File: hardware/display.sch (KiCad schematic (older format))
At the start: 16 parts

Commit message: hardware development
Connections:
- net S1_A: now also U?.7 (A)
- net S1_B: now also U?.6 (B)
- net S1_C: now also U?.4 (C)
- net S1_D: now also U?.2 (D)
- net S1_DP: now also U?.5 (DP)
- net S1_E: now also U?.1 (E)
- net S1_F: now also U?.9 (F)
- net S1_G: now also U?.10 (G)
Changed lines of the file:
@@
 $Descr A4 11693 8268
 encoding utf-8
-Sheet 3 3
+Sheet 2 4
 Title ""
 Date ""
@@
 Wire Wire Line
 	7400 5250 7700 5250
+Wire Wire Line
+	2100 2850 2350 2850
+Wire Wire Line
+	2350 2950 2100 2950
+Wire Wire Line
+	2100 3050 2350 3050
+Wire Wire Line
+	2350 3150 2100 3150
+Wire Wire Line
+	2350 3250 2100 3250
+Wire Wire Line
+	2100 3350 2350 3350
+Wire Wire Line
+	2350 3450 2100 3450
+Wire Wire Line
+	2100 3550 2350 3550
 $EndSCHEMATC

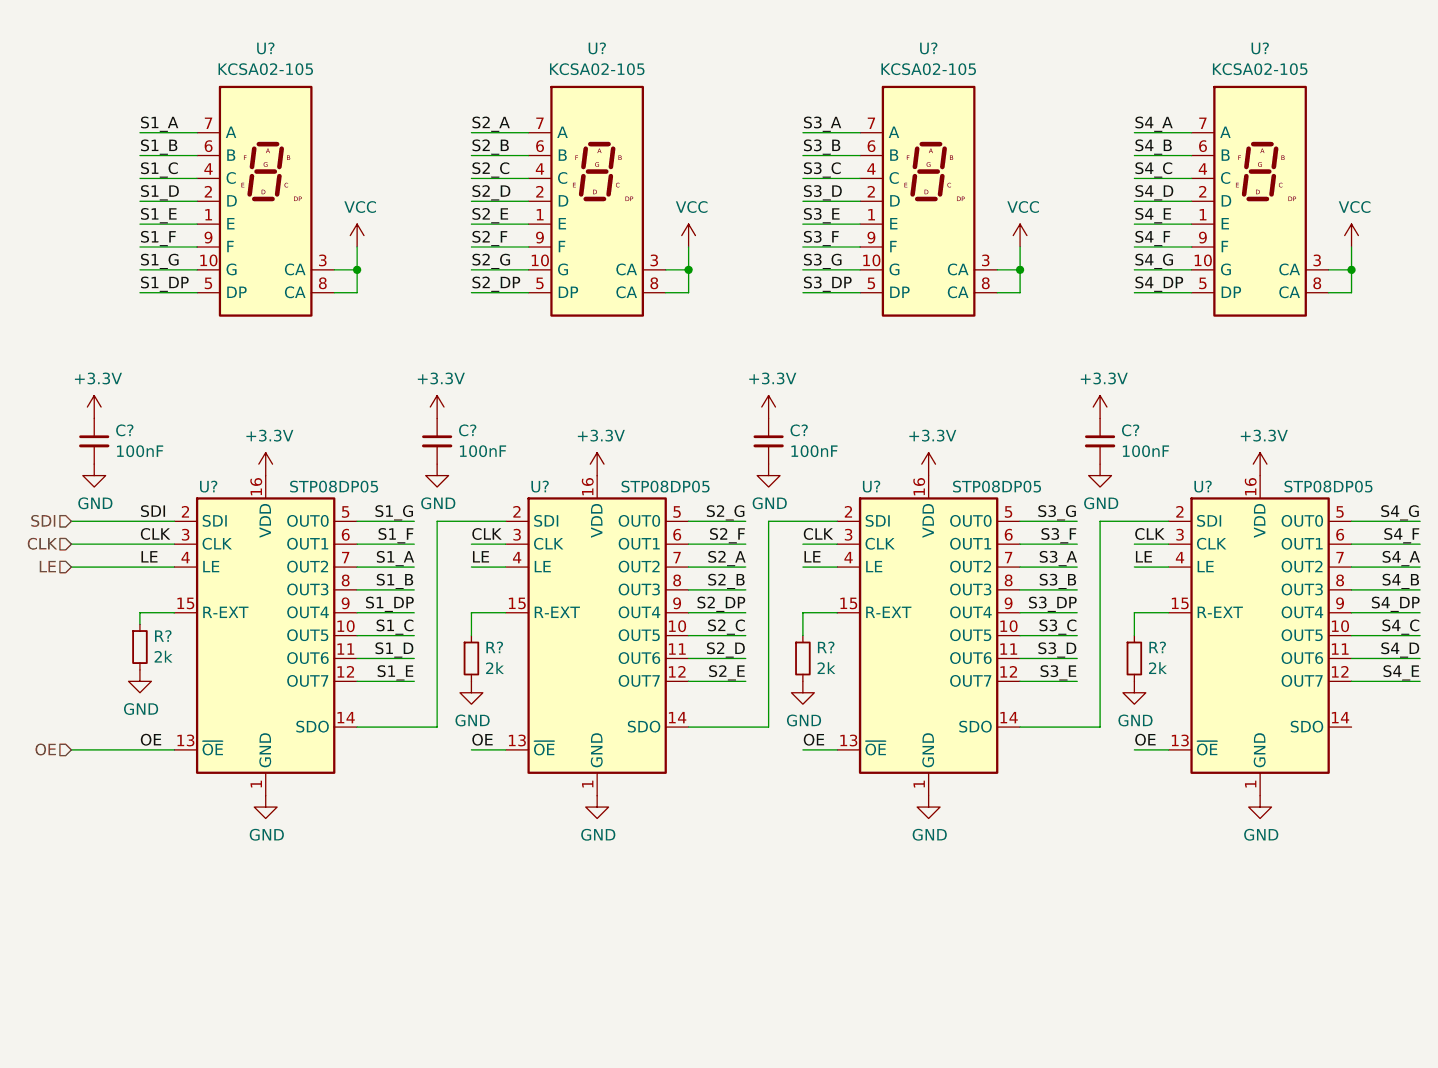
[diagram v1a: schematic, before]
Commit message: schematic should be done, pcb is next
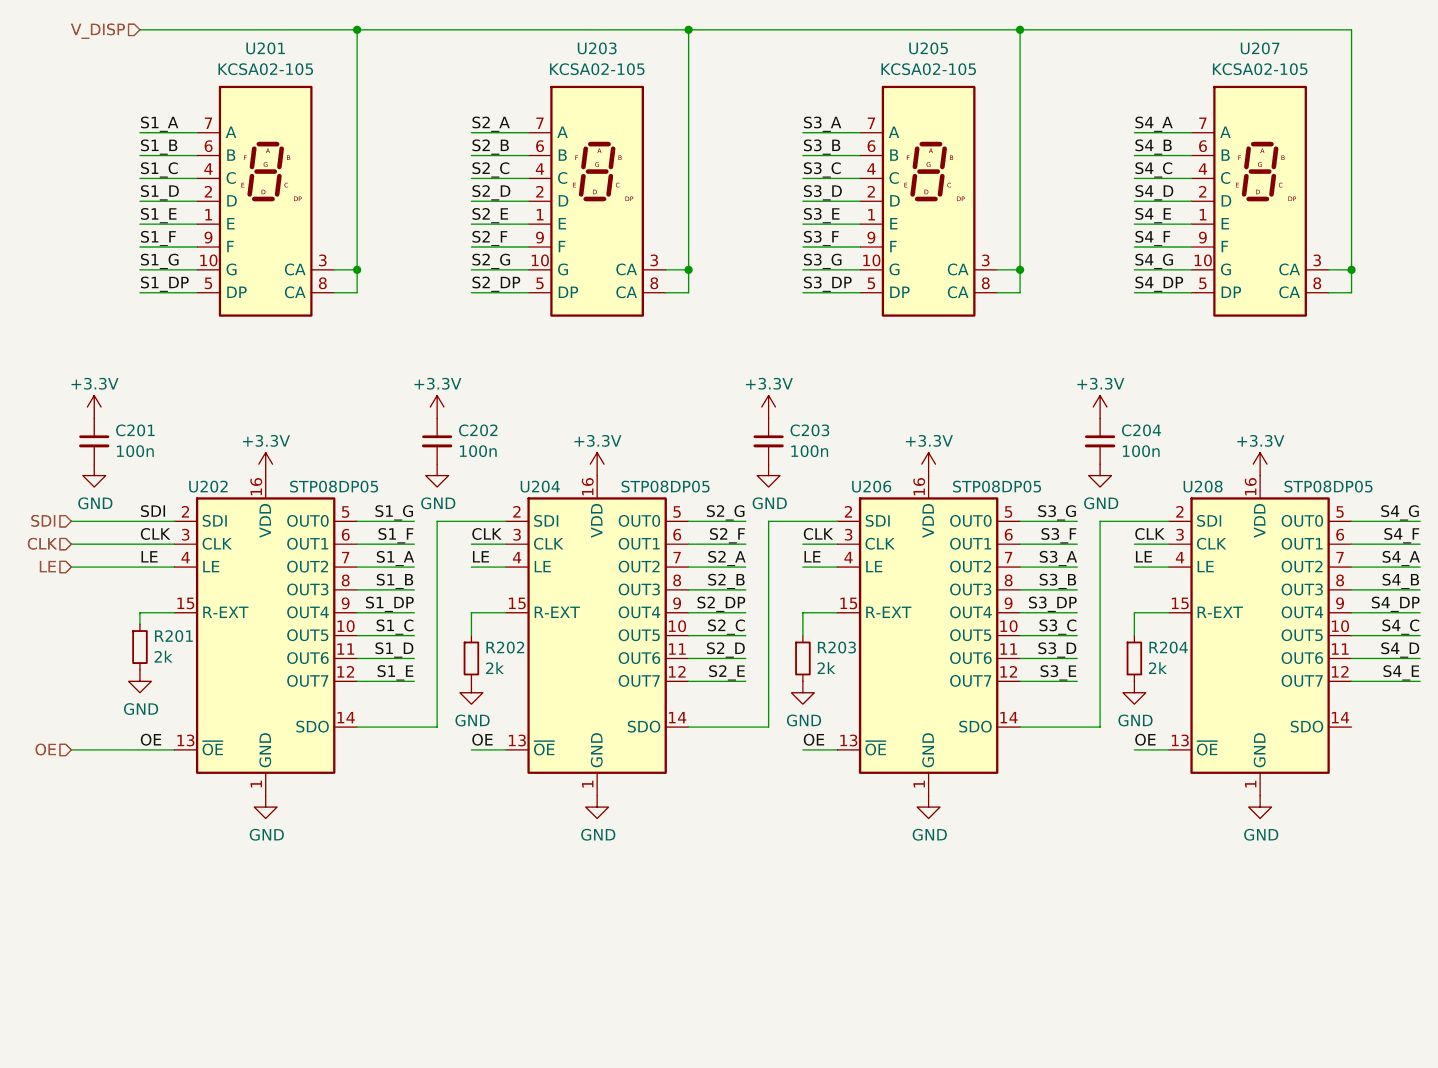
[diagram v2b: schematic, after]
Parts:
- C201, C202, C203, C204: renamed from C?; value 100nF -> 100n; Manufacturer (none) -> KEMET; Order https://www.digikey.at/product-detail/de/kemet/C0603C104M4R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 -> https://www.mouser.at/ProductDetail/80-C0603C104M4R
- R201, R202, R203, R204: renamed from R?; Manufacturer (none) -> Panasonic; Order https://www.digikey.at/product-detail/de/panasonic-electron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 -> https://www.mouser.at/ProductDetail/667-ERJ-PA3F2001V
- U201, U203, U205, U207: renamed from U?; Manufacturer (none) -> Kingbright; Order https://www.digikey.at/product-detail/de/XZFMDK05A/1497-109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 -> https://www.mouser.at/ProductDetail/604-ACSA02-41SURKWA
- U202, U204, U206, U208: renamed from U?; Manufacturer (none) -> STMicroelectornics; Order https://www.digikey.at/product-detail/de/STP08DP05TTR/497-6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 -> https://www.mouser.at/ProductDetail/511-STP08DP05TTR; Part Number (none) -> STP08DP05TTR
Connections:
- net VCC renamed V_DISP

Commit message: wip hw
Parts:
- C201, C202, C203, C204: footprint Capacitor_SMD:C_0603_1608Metric_Pad1.05x0.95mm_HandSolder -> Capacitor_SMD:C_0603_1608Metric
- R201, R202, R203, R204: footprint Resistor_SMD:R_0603_1608Metric_Pad1.05x0.95mm_HandSolder -> Resistor_SMD:R_0603_1608Metric
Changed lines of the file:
@@
 F 0 "R201" H 2159 5146 50  0000 L CNN
 F 1 "2k" H 2159 5055 50  0000 L CNN
-F 2 "Resistor_SMD:R_0603_1608Metric_Pad1.05x0.95mm_HandSolder" H 2100 5100 50  0001 C CNN
+F 2 "Resistor_SMD:R_0603_1608Metric" H 2100 5100 50  0001 C CNN
 F 3 "https://www.mouser.at/datasheet/2/315/AOA0000C331-1141874.pdf" H 2100 5100 50  0001 C CNN
 F 4 "https://www.mouser.at/ProductDetail/667-ERJ-PA3F2001V" H 2100 5100 50  0001 C CNN "Order"
@@
 F 0 "C201" H 1992 4246 50  0000 L CNN
 F 1 "100n" H 1992 4155 50  0000 L CNN
-F 2 "Capacitor_SMD:C_0603_1608Metric_Pad1.05x0.95mm_HandSolder" H 1900 4200 50  0001 C CNN
+F 2 "Capacitor_SMD:C_0603_1608Metric" H 1900 4200 50  0001 C CNN
 F 3 "https://www.mouser.at/datasheet/2/212/KEM_C1002_X7R_SMD-1102033.pdf" H 1900 4200 50  0001 C CNN
 F 4 "https://www.mouser.at/ProductDetail/80-C0603C104M4R" H 1900 4200 50  0001 C CNN "Order"
@@
 F 0 "R202" H 3609 5196 50  0000 L CNN
 F 1 "2k" H 3609 5105 50  0000 L CNN
-F 2 "Resistor_SMD:R_0603_1608Metric_Pad1.05x0.95mm_HandSolder" H 3550 5150 50  0001 C CNN
+F 2 "Resistor_SMD:R_0603_1608Metric" H 3550 5150 50  0001 C CNN
 F 3 "https://www.mouser.at/datasheet/2/315/AOA0000C331-1141874.pdf" H 3550 5150 50  0001 C CNN
 F 4 "https://www.mouser.at/ProductDetail/667-ERJ-PA3F2001V" H 3550 5150 50  0001 C CNN "Order"
@@
 F 0 "R203" H 5059 5196 50  0000 L CNN
 F 1 "2k" H 5059 5105 50  0000 L CNN
-F 2 "Resistor_SMD:R_0603_1608Metric_Pad1.05x0.95mm_HandSolder" H 5000 5150 50  0001 C CNN
+F 2 "Resistor_SMD:R_0603_1608Metric" H 5000 5150 50  0001 C CNN
 F 3 "https://www.mouser.at/datasheet/2/315/AOA0000C331-1141874.pdf" H 5000 5150 50  0001 C CNN
 F 4 "https://www.mouser.at/ProductDetail/667-ERJ-PA3F2001V" H 5000 5150 50  0001 C CNN "Order"
@@
 F 0 "R204" H 6509 5196 50  0000 L CNN
 F 1 "2k" H 6509 5105 50  0000 L CNN
-F 2 "Resistor_SMD:R_0603_1608Metric_Pad1.05x0.95mm_HandSolder" H 6450 5150 50  0001 C CNN
+F 2 "Resistor_SMD:R_0603_1608Metric" H 6450 5150 50  0001 C CNN
 F 3 "https://www.mouser.at/datasheet/2/315/AOA0000C331-1141874.pdf" H 6450 5150 50  0001 C CNN
 F 4 "https://www.mouser.at/ProductDetail/667-ERJ-PA3F2001V" H 6450 5150 50  0001 C CNN "Order"
@@
 F 0 "C202" H 3492 4246 50  0000 L CNN
 F 1 "100n" H 3492 4155 50  0000 L CNN
-F 2 "Capacitor_SMD:C_0603_1608Metric_Pad1.05x0.95mm_HandSolder" H 3400 4200 50  0001 C CNN
+F 2 "Capacitor_SMD:C_0603_1608Metric" H 3400 4200 50  0001 C CNN
 F 3 "https://www.mouser.at/datasheet/2/212/KEM_C1002_X7R_SMD-1102033.pdf" H 3400 4200 50  0001 C CNN
 F 4 "https://www.mouser.at/ProductDetail/80-C0603C104M4R" H 3400 4200 50  0001 C CNN "Order"
@@
 F 0 "C203" H 4942 4246 50  0000 L CNN
 F 1 "100n" H 4942 4155 50  0000 L CNN
-F 2 "Capacitor_SMD:C_0603_1608Metric_Pad1.05x0.95mm_HandSolder" H 4850 4200 50  0001 C CNN
+F 2 "Capacitor_SMD:C_0603_1608Metric" H 4850 4200 50  0001 C CNN
 F 3 "https://www.mouser.at/datasheet/2/212/KEM_C1002_X7R_SMD-1102033.pdf" H 4850 4200 50  0001 C CNN
 F 4 "https://www.mouser.at/ProductDetail/80-C0603C104M4R" H 4850 4200 50  0001 C CNN "Order"
@@
 F 0 "C204" H 6392 4246 50  0000 L CNN
 F 1 "100n" H 6392 4155 50  0000 L CNN
-F 2 "Capacitor_SMD:C_0603_1608Metric_Pad1.05x0.95mm_HandSolder" H 6300 4200 50  0001 C CNN
+F 2 "Capacitor_SMD:C_0603_1608Metric" H 6300 4200 50  0001 C CNN
 F 3 "https://www.mouser.at/datasheet/2/212/KEM_C1002_X7R_SMD-1102033.pdf" H 6300 4200 50  0001 C CNN
 F 4 "https://www.mouser.at/ProductDetail/80-C0603C104M4R" H 6300 4200 50  0001 C CNN "Order"

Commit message: finished routing
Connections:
- no-connect marks 0 -> 1
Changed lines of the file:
@@
 Wire Wire Line
 	5950 2400 7400 2400
+NoConn ~ 7400 5450
 $EndSCHEMATC

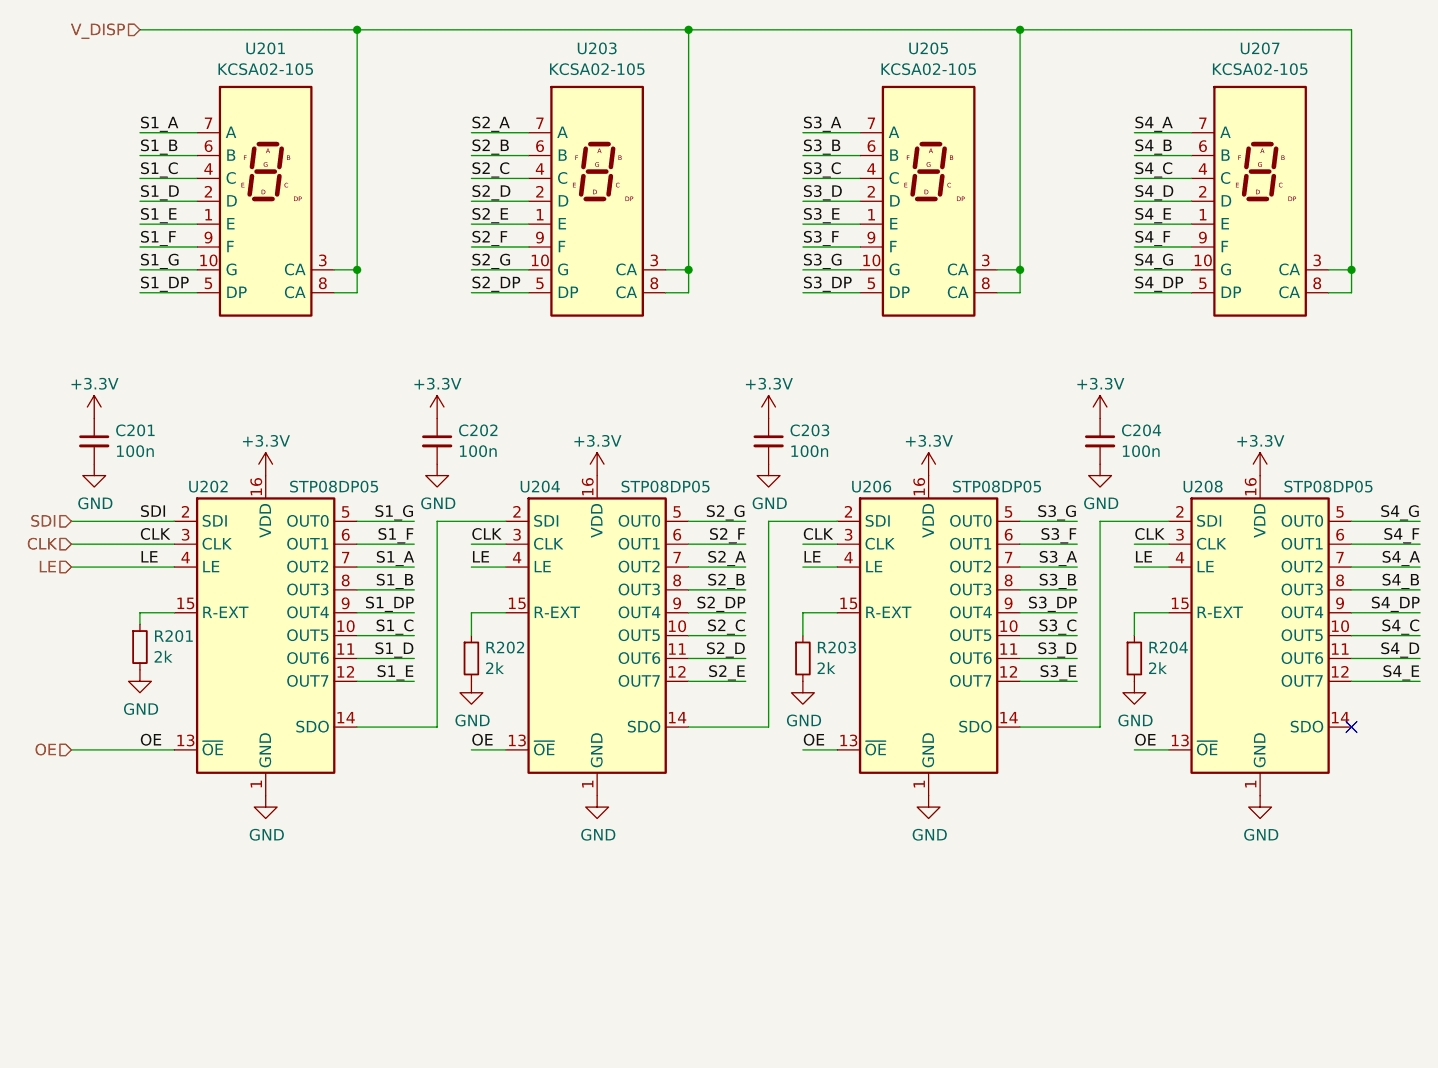
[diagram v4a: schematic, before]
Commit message: calc current consumption
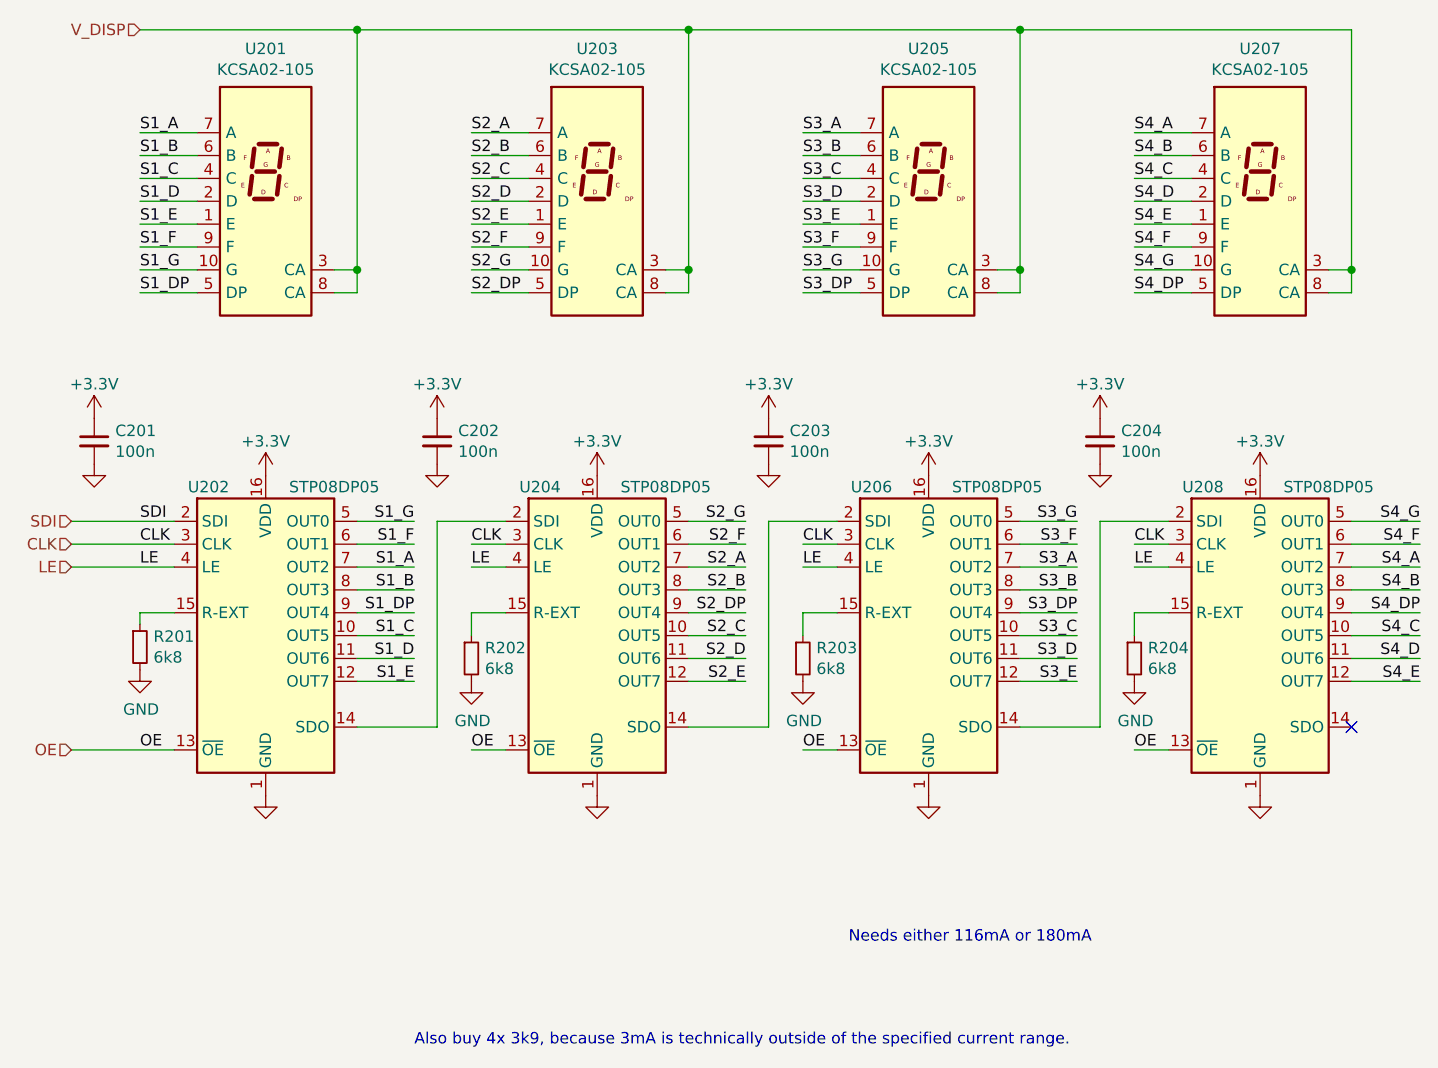
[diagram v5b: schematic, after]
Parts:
- R201, R202, R203, R204: value 2k -> 6k8
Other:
- note added: "Also buy 4x 3k9, because 3mA is technically outside of the specified current range."
- note added: "Needs either 116mA or 180mA"
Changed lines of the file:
@@
 AR Path="/60633D5C/60642EB2" Ref="R201"  Part="1"
 F 0 "R201" H 2159 5146 50  0000 L CNN
-F 1 "2k" H 2159 5055 50  0000 L CNN
+F 1 "6k8" H 2159 5055 50  0000 L CNN
 F 2 "Resistor_SMD:R_0603_1608Metric" H 2100 5100 50  0001 C CNN
 F 3 "https://www.mouser.at/datasheet/2/315/AOA0000C331-1141874.pdf" H 2100 5100 50  0001 C CNN
@@
 AR Path="/60633D5C/60642EC3" Ref="#PWR0102"  Part="1"
 F 0 "#PWR0102" H 1900 4050 50  0001 C CNN
-F 1 "GND" H 1905 4127 50  0000 C CNN
+F 1 "GND" H 1905 4127 50  0001 C CNN
 F 2 "" H 1900 4300 50  0001 C CNN
 F 3 "" H 1900 4300 50  0001 C CNN
@@
 AR Path="/60633D5C/60642EC9" Ref="#PWR0103"  Part="1"
 F 0 "#PWR0103" H 2650 5500 50  0001 C CNN
-F 1 "GND" H 2655 5577 50  0000 C CNN
+F 1 "GND" H 2655 5577 50  0001 C CNN
 F 2 "" H 2650 5750 50  0001 C CNN
 F 3 "" H 2650 5750 50  0001 C CNN
@@
 AR Path="/60633D5C/60642EFF" Ref="#PWR0108"  Part="1"
 F 0 "#PWR0108" H 4100 5500 50  0001 C CNN
-F 1 "GND" H 4105 5577 50  0000 C CNN
+F 1 "GND" H 4105 5577 50  0001 C CNN
 F 2 "" H 4100 5750 50  0001 C CNN
 F 3 "" H 4100 5750 50  0001 C CNN
@@
 AR Path="/60633D5C/60642F0C" Ref="R202"  Part="1"
 F 0 "R202" H 3609 5196 50  0000 L CNN
-F 1 "2k" H 3609 5105 50  0000 L CNN
+F 1 "6k8" H 3609 5105 50  0000 L CNN
 F 2 "Resistor_SMD:R_0603_1608Metric" H 3550 5150 50  0001 C CNN
 F 3 "https://www.mouser.at/datasheet/2/315/AOA0000C331-1141874.pdf" H 3550 5150 50  0001 C CNN
@@
 AR Path="/60633D5C/60642F27" Ref="#PWR0111"  Part="1"
 F 0 "#PWR0111" H 5550 5500 50  0001 C CNN
-F 1 "GND" H 5555 5577 50  0000 C CNN
+F 1 "GND" H 5555 5577 50  0001 C CNN
 F 2 "" H 5550 5750 50  0001 C CNN
 F 3 "" H 5550 5750 50  0001 C CNN
@@
 AR Path="/60633D5C/60642F34" Ref="R203"  Part="1"
 F 0 "R203" H 5059 5196 50  0000 L CNN
-F 1 "2k" H 5059 5105 50  0000 L CNN
+F 1 "6k8" H 5059 5105 50  0000 L CNN
 F 2 "Resistor_SMD:R_0603_1608Metric" H 5000 5150 50  0001 C CNN
 F 3 "https://www.mouser.at/datasheet/2/315/AOA0000C331-1141874.pdf" H 5000 5150 50  0001 C CNN
@@
 AR Path="/60633D5C/60642F4F" Ref="#PWR0114"  Part="1"
 F 0 "#PWR0114" H 7000 5500 50  0001 C CNN
-F 1 "GND" H 7005 5577 50  0000 C CNN
+F 1 "GND" H 7005 5577 50  0001 C CNN
 F 2 "" H 7000 5750 50  0001 C CNN
 F 3 "" H 7000 5750 50  0001 C CNN
@@
 AR Path="/60633D5C/60642F5C" Ref="R204"  Part="1"
 F 0 "R204" H 6509 5196 50  0000 L CNN
-F 1 "2k" H 6509 5105 50  0000 L CNN
+F 1 "6k8" H 6509 5105 50  0000 L CNN
 F 2 "Resistor_SMD:R_0603_1608Metric" H 6450 5150 50  0001 C CNN
 F 3 "https://www.mouser.at/datasheet/2/315/AOA0000C331-1141874.pdf" H 6450 5150 50  0001 C CNN
@@
 AR Path="/60633D5C/606457A9" Ref="#PWR0116"  Part="1"
 F 0 "#PWR0116" H 3400 4050 50  0001 C CNN
-F 1 "GND" H 3405 4127 50  0000 C CNN
+F 1 "GND" H 3405 4127 50  0001 C CNN
 F 2 "" H 3400 4300 50  0001 C CNN
 F 3 "" H 3400 4300 50  0001 C CNN
@@
 AR Path="/60633D5C/60646EB7" Ref="#PWR0118"  Part="1"
 F 0 "#PWR0118" H 4850 4050 50  0001 C CNN
-F 1 "GND" H 4855 4127 50  0000 C CNN
+F 1 "GND" H 4855 4127 50  0001 C CNN
 F 2 "" H 4850 4300 50  0001 C CNN
 F 3 "" H 4850 4300 50  0001 C CNN
@@
 AR Path="/60633D5C/60647DB5" Ref="#PWR0120"  Part="1"
 F 0 "#PWR0120" H 6300 4050 50  0001 C CNN
-F 1 "GND" H 6305 4127 50  0000 C CNN
+F 1 "GND" H 6305 4127 50  0001 C CNN
 F 2 "" H 6300 4300 50  0001 C CNN
 F 3 "" H 6300 4300 50  0001 C CNN
@@
 	5950 2400 7400 2400
 NoConn ~ 7400 5450
+Text Notes 3300 6850 0    50   ~ 0
+Also buy 4x 3k9, because 3mA is technically outside of the specified current range.
+Text Notes 5200 6400 0    50   ~ 0
+Needs either 116mA or 180mA
 $EndSCHEMATC
